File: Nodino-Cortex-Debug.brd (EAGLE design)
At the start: 27.9 x 25.4 mm, 12 parts, among them CON1 NODINO-JTAGMODULE, CON2 USB-OTG_SHIELD, IC1 FT2232D, IC2 AP733333SAG, Q1 16MHz

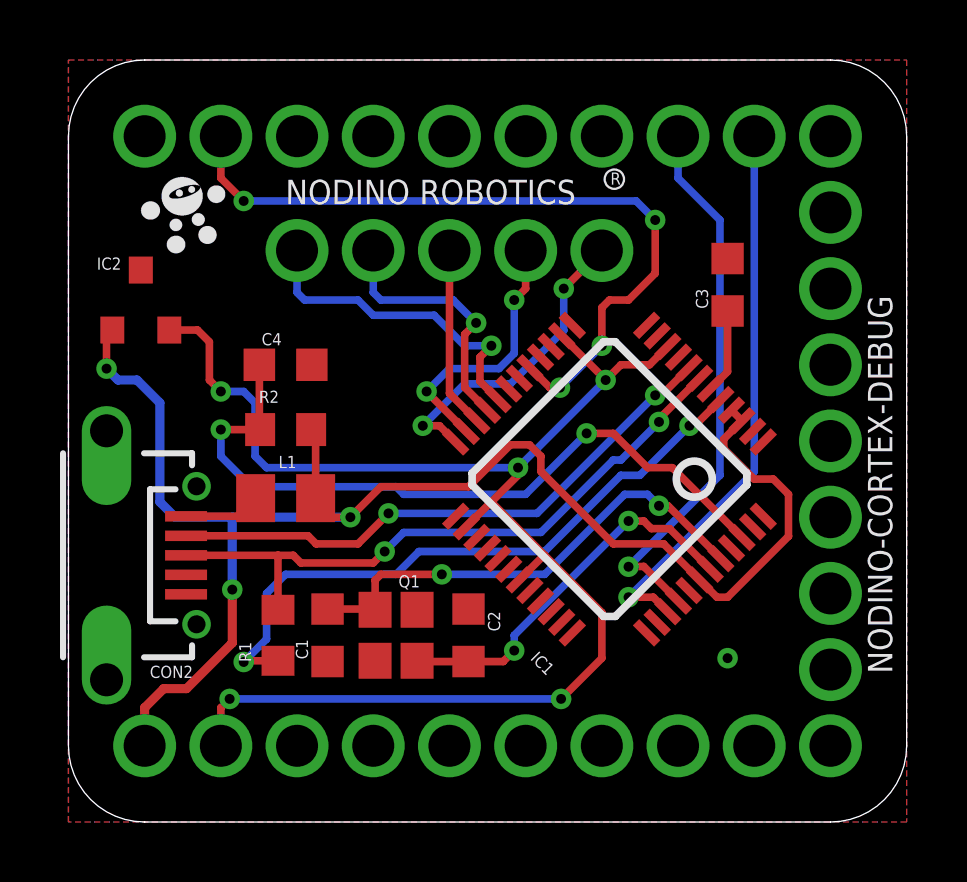
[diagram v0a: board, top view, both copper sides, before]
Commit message: swap TXD and RXD, added filter capacitors
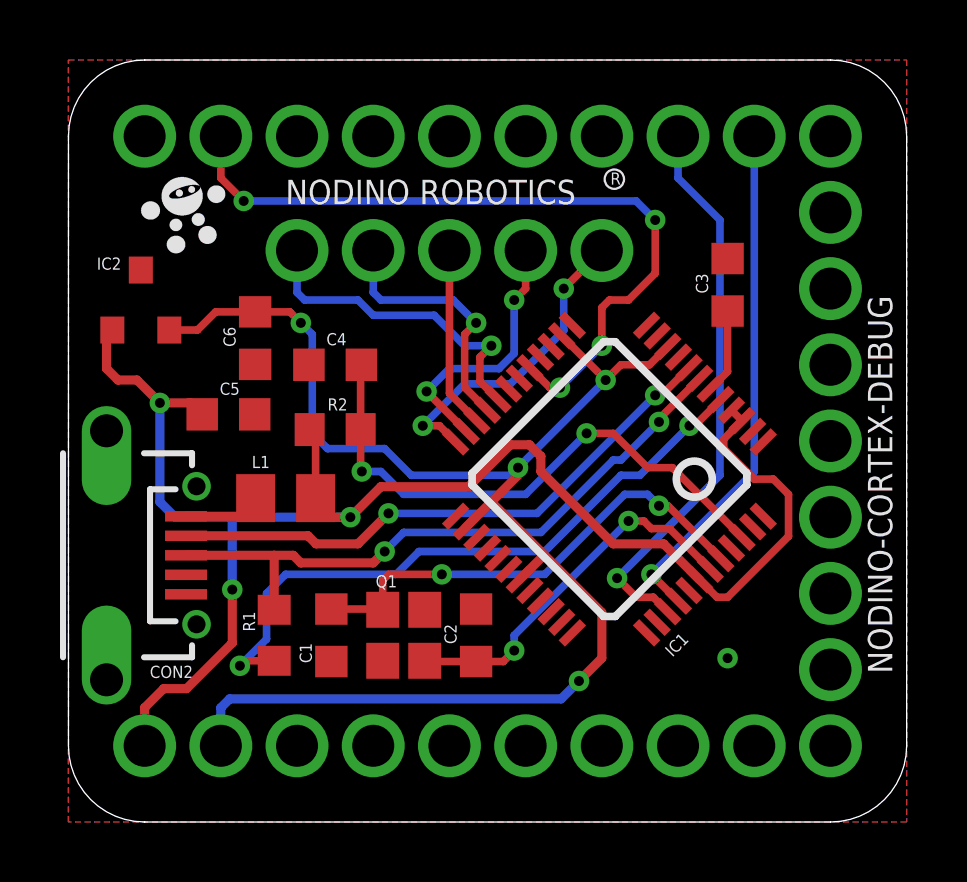
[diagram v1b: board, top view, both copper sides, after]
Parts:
- added C5, C6: 10uF, resistor:C0603K
- moved C4 1.65 mm to (8.89, 15.2), turned to 180 degrees
- moved R2 1.65 mm to (8.89, 13.1), turned to 180 degrees
- moved C2 0.25 mm to (13.6, 6.22)
- moved Q1 0.25 mm to (11.2, 6.22)
- moved C1 0.13 mm to (8.76, 6.22)
- moved R1 0.13 mm to (6.86, 6.22)
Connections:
- removed net USART_RX: CON1.19, IC1.39
- removed net USART_TX: CON1.20, IC1.40
- new net RXD: CON1.20, IC1.39
- new net TXD: CON1.19, IC1.40
- net +3V3: now also C6.1
- net +5V: now also C5.1
- net GND: now also C5.2, C6.2
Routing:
- net RXD: track 0.00 -> 18.9 mm, vias 0 -> 1
- net USART_RX: track 18.6 -> 0.00 mm, vias 1 -> 0
- net USART_TX: track 18.3 -> 0.00 mm, vias 1 -> 0
- net TXD: track 0.00 -> 17.3 mm, vias 0 -> 1
- net N$14: track 24.5 -> 18.9 mm
- net +5V: track 51.3 -> 52.9 mm
- net +3V3: track 49.4 -> 50.3 mm, vias 5 -> 4

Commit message: minor fix to crystal value typo from 16MHz to 6MHz
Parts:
- Q1: value 16MHz -> 6MHz
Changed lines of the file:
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@@
 <elements>
 <element name="CON1" library="nodino" package="NODINO-JTAG-MOD" value="NODINO-JTAGMODULE" x="13.97" y="12.7" smashed="yes"/>
-<element name="Q1" library="crystal" package="FA-20H" value="16MHz" x="11.176" y="6.223" smashed="yes" rot="R270">
+<element name="Q1" library="crystal" package="FA-20H" value="6MHz" x="11.176" y="6.223" smashed="yes" rot="R270">
 <attribute name="NAME" x="10.239" y="7.82" size="0.4064" layer="25"/>
 <attribute name="VALUE" x="11.991" y="4.655" size="0.4064" layer="27" rot="R180"/>
